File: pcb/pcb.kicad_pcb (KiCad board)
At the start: 2 copper layers, 81 x 80 mm, 11 parts, among them U1 PCF8883

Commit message: add repo url text on bottom
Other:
- board text added: "https://github.com/urish/panda"
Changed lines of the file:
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@@
     (area 98.929348 34.911247 180.026456 120.181153)
     (thickness 1.6)
-    (drawings 142)
+    (drawings 143)
     (tracks 61)
     (zones 0)
@@
       (layerselection 0x010f0_80000001)
       (usegerberextensions true)
-      (excludeedgelayer false)
-      (linewidth 0.076200)
+      (excludeedgelayer true)
+      (linewidth 0.020000)
       (plotframeref false)
       (viasonmask false)
@@
     )
   )
+  (gr_text https://github.com/urish/panda (at 173.99 72.898 288) (layer B.SilkS)
+    (effects (font (size 1 1) (thickness 0.2)) (justify mirror))
+  )
   (gr_line (start 158.851335 67.041243) (end 158.851335 67.041243) (layer Edge.Cuts) (width 0.1))

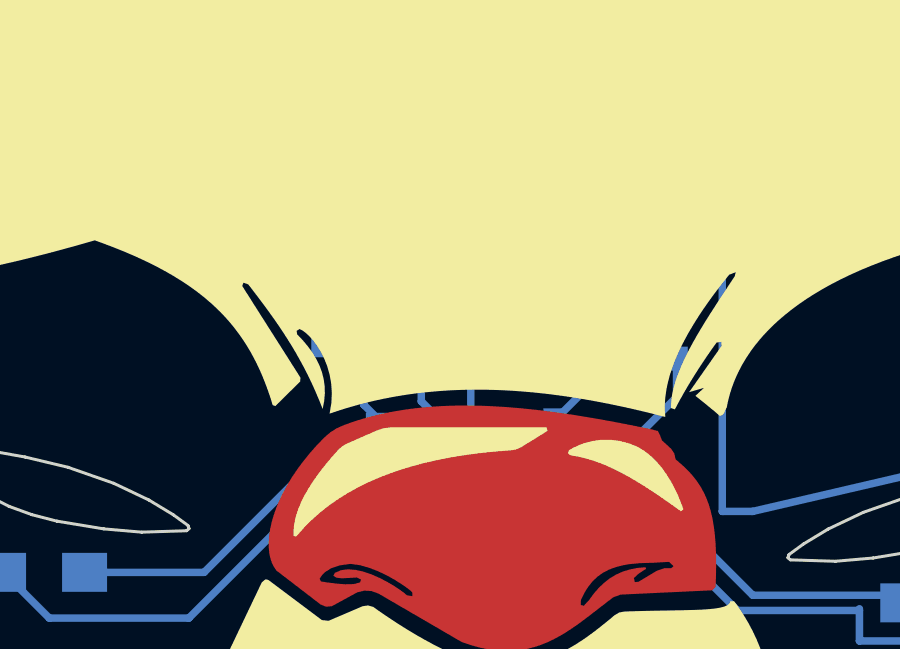
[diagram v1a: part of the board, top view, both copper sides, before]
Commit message: set PCF8883 to switch mode
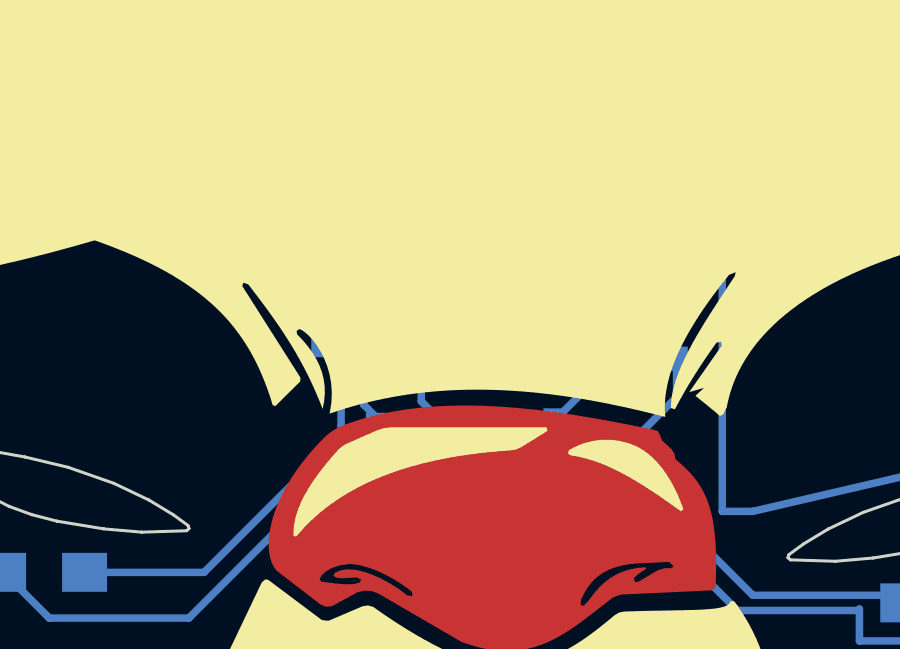
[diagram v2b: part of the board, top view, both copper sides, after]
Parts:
- Cf1: renamed from Cf; value C -> 10pF
- Rc1: renamed from Rc; value R -> 100k
- Rf1: renamed from Rf; value R -> 1k
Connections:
- C2 pad 1: Net-(C2-Pad1) -> VREGINT
- U1 pad 2: GND -> VREGINT
- U1 pad 8: Net-(C2-Pad1) -> VREGINT
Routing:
- net VREGINT: track 0.00 -> 10.1 mm
- net Net-(C2-Pad1): track 3.21 -> 0.00 mm
